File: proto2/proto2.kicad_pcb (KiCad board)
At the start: 2 copper layers, 245.9 x 132.5 mm, 239 parts, among them J1 Output 1, J10 Output, J11 Device, J12 Output, J13 Daughter Card, J2 Main Power, J3 Output, J4 Output, J5 Device, J6 Output, J7 Device, J8 Output, J9 Device, Q1 2N7002, Q10 2N7002, Q11 2N7002, Q12 2N7002, Q13 2N7002, Q14 2N7002, Q2 2N7002, Q3 2N7002, Q4 2N7002, Q5 2N7002, Q6 2N7002, Q7 2N7002, Q8 2N7002, Q9 2N7002, SW1 SW_DIP_x04, U1 AQY282SX, U10 AQY282SX, U11 AQY282SX, U12 AQY282SX, U13 AQY282SX, U14 AQY282SX, U15 NCP59300, U2 AQY282SX, U3 AQY282SX, U4 AQY282SX, U5 AQY282SX, U6 AQY282SX, U7 AQY282SX, U8 AQY282SX, U9 AQY282SX

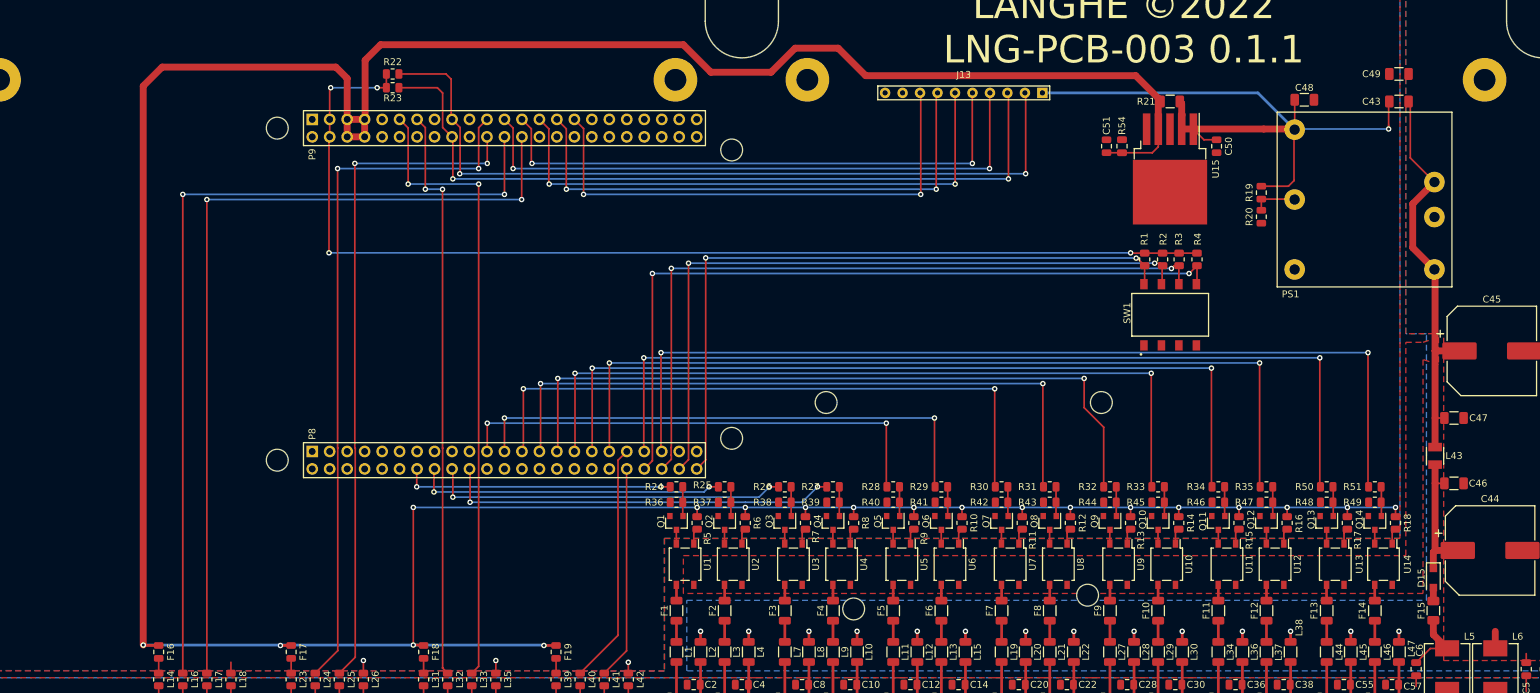
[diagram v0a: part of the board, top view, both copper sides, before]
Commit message: Added switch for 5V external devices power based off SYS_RESETn.
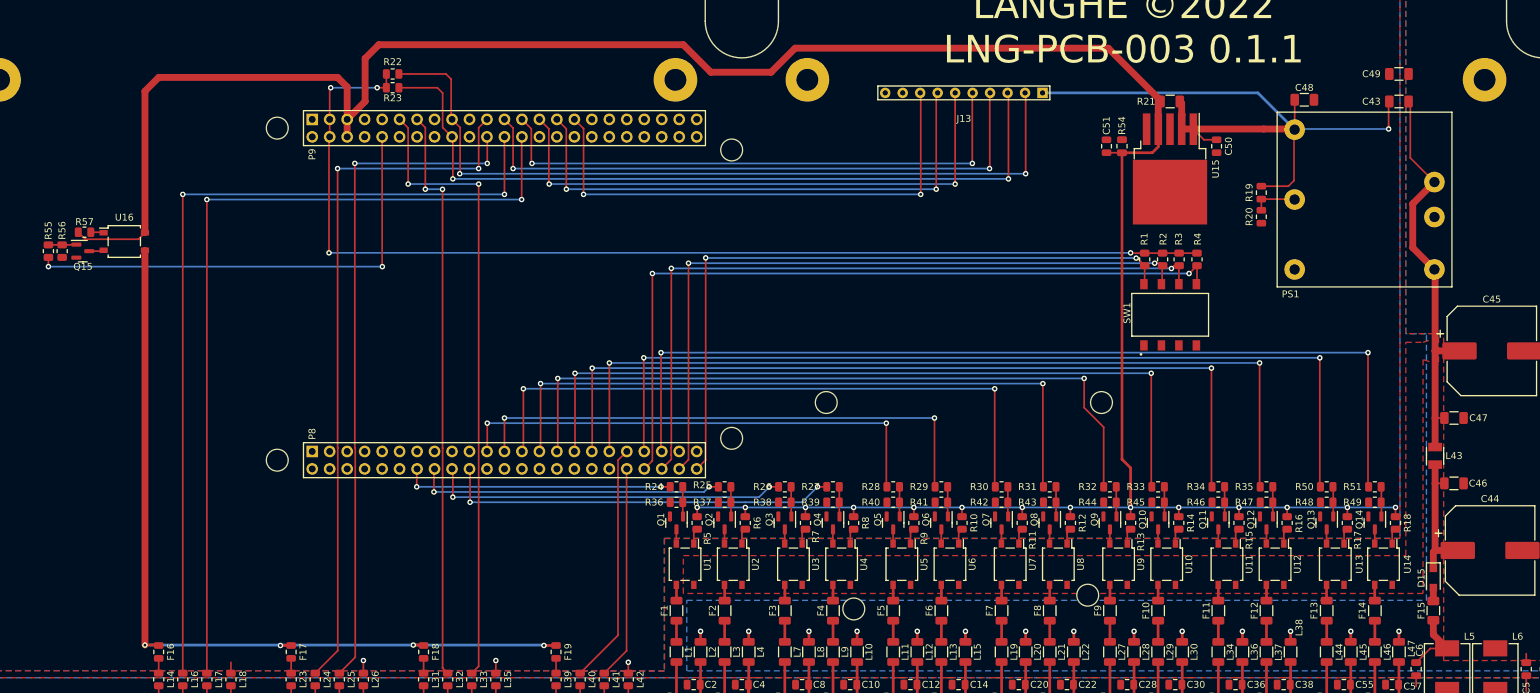
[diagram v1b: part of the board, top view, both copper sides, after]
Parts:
- added Q15: 2N7002, Package_TO_SOT_SMD:SOT-23, F.Cu at (17.0, 81.0)
- added R55: 1K, Resistor_SMD:R_0805_2012Metric, F.Cu at (12.0, 81.0)
- added R56: 27K, Resistor_SMD:R_0805_2012Metric, F.Cu at (14.0, 81.0)
- added R57: 433R, Resistor_SMD:R_0805_2012Metric, F.Cu at (17.2, 78.2)
- added U16: AQY282SX, Package_SO:SO-4_4.4x4.3mm_P2.54mm, F.Cu at (23.0, 79.6)
- D15: value SMA -> D_Small_ALT
- Q13, Q14: footprint Package_BCR:SOT-23 -> Package_TO_SOT_SMD:SOT-23
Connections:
- BB1 pad 9.10: unconnected-(BB1-Pad9.10) -> RESETn
- BB1 pad 9.7: +5V -> unconnected-(BB1-Pad9.7)
- BB1 pad 9.8: +5V -> unconnected-(BB1-Pad9.8)
- F16 pad 2: +5V -> +5VP
- F17 pad 2: +5V -> +5VP
- F18 pad 2: +5V -> +5VP
- F19 pad 2: +5V -> +5VP
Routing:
- net +5V: track 523.2 -> 390.2 mm, vias 19 -> 14
- net +5VP: track 0.00 -> 122.2 mm, vias 0 -> 4
- net RESETn: track 0.00 -> 68.7 mm, vias 0 -> 2
- net Net-(Q15-Pad1): track 0.00 -> 4.08 mm
- net Earth: track 28.2 -> 25.7 mm
- net Net-(Q15-Pad3): track 0.00 -> 2.15 mm
- net Net-(R57-Pad1): track 0.00 -> 1.90 mm

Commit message: Working in suggestions from CFL review.
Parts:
- removed C50: 1uF, Capacitor_SMD:C_0805_2012Metric
- removed R21: 0R, Capacitor_SMD:C_1206_3216Metric
- removed U15: NCP59300, Package_TO_SOT_SMD:TO-263-5_TabPin3
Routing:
- net +5V: track 390.2 -> 195.2 mm
- net VDD: track 98.1 -> 0.75 mm, vias 1 -> 0
- net +5VP: track 122.2 -> 64.8 mm
- net GND: vias 5 -> 6
- added copper zone on In2.Cu, net +5V
- added copper zone on In1.Cu, net GND
- removed copper zone on F.Cu, net GND
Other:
- copper layers 2 -> 4

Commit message: Laying out new filters and some schematic updates.
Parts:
- removed F16, F17, F18, F19: 500mA, Resistor_SMD:R_0805_2012Metric
- removed the J1 at (108.5, 152.5)
- removed the J10 at (187.2, 152.5)
- removed the J12 at (203.0, 152.5)
- removed L37, L38, L44, L45, L46, L47: 1A Ferrite, Resistor_SMD:R_1206_3216Metric
- removed L40, L41: 0R, Resistor_SMD:R_0805_2012Metric
- removed REF**: Langhe_Carrot, BCR_Art:Langhe_Carrot
- removed U16: AQY282SX, Package_SO:SO-4_4.4x4.3mm_P2.54mm
- added C50: 10uF, Capacitor_SMD:C_0805_2012Metric, F.Cu at (134.0, 243.2)
- added C58: 10uF, Capacitor_SMD:C_0805_2012Metric, F.Cu at (86.4, 291.4)
- added C59: 10uF, Capacitor_SMD:C_0805_2012Metric, F.Cu at (99.7, 291.4)
- added C60: 10uF, Capacitor_SMD:C_0805_2012Metric, F.Cu at (154.2, 232.2)
- added C61: 10uF, Capacitor_SMD:C_0805_2012Metric, F.Cu at (103.2, 282.4)
- added C62: 10uF, Capacitor_SMD:C_0805_2012Metric, F.Cu at (137.3, 249.0)
- added C63: 10uF, Capacitor_SMD:C_0805_2012Metric, F.Cu at (154.2, 235.2)
- added C64: 10uF, Capacitor_SMD:C_0805_2012Metric, F.Cu at (90.8, 294.4)
- added C65: 10uF, Capacitor_SMD:C_0805_2012Metric, F.Cu at (86.4, 297.4)
- added C66: 10uF, Capacitor_SMD:C_0805_2012Metric, F.Cu at (141.8, 255.0)
- added C67: 10uF, Capacitor_SMD:C_0805_2012Metric, F.Cu at (140.6, 261.1)
- added C68: 10uF, Capacitor_SMD:C_0805_2012Metric, F.Cu at (158.6, 235.2)
- added C69: 10uF, Capacitor_SMD:C_0805_2012Metric, F.Cu at (122.2, 277.6)
- added C70: 10uF, Capacitor_SMD:C_0805_2012Metric, F.Cu at (95.3, 294.4)
- added C71: 10uF, Capacitor_SMD:C_0805_2012Metric, F.Cu at (95.3, 291.4)
- added C72: 10uF, Capacitor_SMD:C_0805_2012Metric, F.Cu at (157.4, 238.2)
- added C73: 10uF, Capacitor_SMD:C_0805_2012Metric, F.Cu at (136.2, 261.1)
- added C74: 10uF, Capacitor_SMD:C_0805_2012Metric, F.Cu at (140.6, 258.1)
- added C75: 10uF, Capacitor_SMD:C_0805_2012Metric, F.Cu at (146.2, 253.8)
- added C76: 10uF, Capacitor_SMD:C_0805_2012Metric, F.Cu at (113.2, 276.9)
- added C77: 10uF, Capacitor_SMD:C_0805_2012Metric, F.Cu at (151.8, 243.6)
- added C78: 10uF, Capacitor_SMD:C_0805_2012Metric, F.Cu at (128.4, 265.5)
- added C79: 10uF, Capacitor_SMD:C_0805_2012Metric, F.Cu at (157.4, 241.2)
- added C80: 10uF, Capacitor_SMD:C_0805_2012Metric, F.Cu at (90.8, 291.4)
- added C81: 10uF, Capacitor_SMD:C_0805_2012Metric, F.Cu at (86.4, 294.4)
- added C82: 10uF, Capacitor_SMD:C_0805_2012Metric, F.Cu at (163.1, 232.2)
- added C83: 10uF, Capacitor_SMD:C_0805_2012Metric, F.Cu at (128.4, 268.5)
- added C84: 10uF, Capacitor_SMD:C_0805_2012Metric, F.Cu at (132.8, 267.1)
- added C85: 10uF, Capacitor_SMD:C_0805_2012Metric, F.Cu at (123.9, 268.5)
- added C86: 10uF, Capacitor_SMD:C_0805_2012Metric, F.Cu at (193.8, 248.4)
- added C87: 10uF, Capacitor_SMD:C_0805_2012Metric, F.Cu at (219.5, 233.2)
- added C88: 10uF, Capacitor_SMD:C_0805_2012Metric, F.Cu at (215.0, 237.0)
- added C89: 10uF, Capacitor_SMD:C_0805_2012Metric, F.Cu at (210.1, 232.8)
- added C90: 10uF, Capacitor_SMD:C_0805_2012Metric, F.Cu at (198.2, 248.4)
- added C91: 10uF, Capacitor_SMD:C_0805_2012Metric, F.Cu at (193.8, 245.4)
- added C92: 10uF, Capacitor_SMD:C_0805_2012Metric, F.Cu at (214.8, 232.2)
- added C93: 10uF, Capacitor_SMD:C_0805_2012Metric, F.Cu at (198.2, 245.4)
- added C94: 10uF, Capacitor_SMD:C_0805_2012Metric, F.Cu at (189.3, 245.4)
- added C95: 10uF, Capacitor_SMD:C_0805_2012Metric, F.Cu at (189.3, 248.4)
- added J2: Output, Connector_BCR:Phoenix_Contact_PST_4, F.Cu at (108.5, 152.5)
- added J5: Output, Connector_BCR:Phoenix_Contact_PST_4, F.Cu at (155.8, 152.5)
- added J7: Output, Connector_BCR:Phoenix_Contact_PST_4, F.Cu at (124.2, 152.5)
- added PS2: B0505S-1WR3, Converter_DCDC:Converter_DCDC_Murata_MEE1SxxxxSC_THT, F.Cu at (209.6, 245.9)
- added PS3: B0505S-1WR3, Converter_DCDC:Converter_DCDC_Murata_MEE1SxxxxSC_THT, F.Cu at (217.4, 245.9)
- added Q16: AO3401A, Package_TO_SOT_SMD:SOT-23, F.Cu at (-26.2, 97.0)
- added R100: 0R, Resistor_SMD:R_0805_2012Metric, F.Cu at (131.0, 278.9)
- added R101: 0R, Resistor_SMD:R_0805_2012Metric, F.Cu at (150.5, 262.7)
- added R102: 0R, Resistor_SMD:R_0805_2012Metric, F.Cu at (150.7, 256.7)
- added R103: 0R, Resistor_SMD:R_0805_2012Metric, F.Cu at (141.6, 269.9)
- added R104: 0R, Resistor_SMD:R_0805_2012Metric, F.Cu at (153.9, 259.6)
- added R105: 0R, Resistor_SMD:R_0805_2012Metric, F.Cu at (108.5, 291.4)
- added R106: 0R, Resistor_SMD:R_0805_2012Metric, F.Cu at (99.6, 306.2)
- added R107: 0R, Resistor_SMD:R_0805_2012Metric, F.Cu at (95.2, 300.4)
- added R108: 0R, Resistor_SMD:R_0805_2012Metric, F.Cu at (90.8, 303.4)
- added R109: 0R, Resistor_SMD:R_0805_2012Metric, F.Cu at (166.3, 238.2)
- added R110: 0R, Resistor_SMD:R_0805_2012Metric, F.Cu at (146.1, 268.6)
- added R111: 0R, Resistor_SMD:R_0805_2012Metric, F.Cu at (125.5, 243.2)
- added R112: 0R, Resistor_SMD:R_0805_2012Metric, F.Cu at (150.7, 250.8)
- added R113: 0R, Resistor_SMD:R_0805_2012Metric, F.Cu at (159.5, 247.2)
- added R114: 0R, Resistor_SMD:R_0805_2012Metric, F.Cu at (163.9, 247.1)
- added R115: 0R, Resistor_SMD:R_0805_2012Metric, F.Cu at (132.0, 243.2)
- added R116: 0R, Resistor_SMD:R_0805_2012Metric, F.Cu at (137.2, 267.0)
- added R117: 0R, Resistor_SMD:R_0805_2012Metric, F.Cu at (112.9, 294.3)
- added R118: 0R, Resistor_SMD:R_0805_2012Metric, F.Cu at (90.8, 300.4)
- added R119: 0R, Resistor_SMD:R_0805_2012Metric, F.Cu at (108.5, 294.3)
- added R120: 0R, Resistor_SMD:R_0805_2012Metric, F.Cu at (99.6, 300.4)
- added R121: 0R, Resistor_SMD:R_0805_2012Metric, F.Cu at (146.2, 256.8)
- added R122: 0R, Resistor_SMD:R_0805_2012Metric, F.Cu at (180.8, 232.2)
- added R123: 0R, Resistor_SMD:R_0805_2012Metric, F.Cu at (176.3, 235.1)
- added R124: 0R, Resistor_SMD:R_0805_2012Metric, F.Cu at (170.7, 238.1)
- added R125: 0R, Resistor_SMD:R_0805_2012Metric, F.Cu at (126.5, 283.4)
- added R126: 0R, Resistor_SMD:R_0805_2012Metric, F.Cu at (159.5, 250.2)
- added R127: 0R, Resistor_SMD:R_0805_2012Metric, F.Cu at (170.7, 244.1)
- added R128: 0R, Resistor_SMD:R_0805_2012Metric, F.Cu at (155.1, 256.1)
- added R129: 0R, Resistor_SMD:R_0805_2012Metric, F.Cu at (166.3, 241.1)
- added R130: 0R, Resistor_SMD:R_0805_2012Metric, F.Cu at (146.1, 262.7)
- added R131: 0R, Resistor_SMD:R_0805_2012Metric, F.Cu at (137.2, 264.0)
- added R132: 0R, Resistor_SMD:R_0805_2012Metric, F.Cu at (171.9, 232.2)
- added R133: 0R, Resistor_SMD:R_0805_2012Metric, F.Cu at (167.5, 235.2)
- added R134: 0R, Resistor_SMD:R_0805_2012Metric, F.Cu at (155.1, 253.1)
- added R135: 0R, Resistor_SMD:R_0805_2012Metric, F.Cu at (187.5, 287.0)
- added R136: 0R, Resistor_SMD:R_0805_2012Metric, F.Cu at (155.1, 247.2)
- added R137: 4.7K, Resistor_SMD:R_0805_2012Metric, F.Cu at (236.2, 233.2)
- added R138: 4.7K, Resistor_SMD:R_0805_2012Metric, F.Cu at (237.5, 245.0)
- added R139: 120R, Resistor_SMD:R_0805_2012Metric, F.Cu at (244.0, 245.2)
- added R140: 120R, Resistor_SMD:R_0805_2012Metric, F.Cu at (236.2, 239.8)
- added R141: 0R, Resistor_SMD:R_0805_2012Metric, F.Cu at (126.6, 277.5)
- added R142: 0R, Resistor_SMD:R_0805_2012Metric, F.Cu at (116.5, 284.8)
- added R143: 0R, Resistor_SMD:R_0805_2012Metric, F.Cu at (161.9, 241.2)
- added R144: 0R, Resistor_SMD:R_0805_2012Metric, F.Cu at (170.7, 241.1)
- added R145: 0R, Resistor_SMD:R_0805_2012Metric, F.Cu at (141.7, 267.0)
- added R146: 0R, Resistor_SMD:R_0805_2012Metric, F.Cu at (131.0, 281.9)
- added R147: 0R, Resistor_SMD:R_0805_2012Metric, F.Cu at (150.7, 253.8)
- added R148: 0R, Resistor_SMD:R_0805_2012Metric, F.Cu at (159.5, 253.1)
- added R149: 0R, Resistor_SMD:R_0805_2012Metric, F.Cu at (121.1, 295.8)
- added R21: 10K, Resistor_SMD:R_0805_2012Metric, F.Cu at (140.1, 291.4)
- added R58: 0R, Resistor_SMD:R_0805_2012Metric, F.Cu at (129.9, 294.3)
- added R59: 0R, Resistor_SMD:R_0805_2012Metric, F.Cu at (130.4, 291.4)
- added R60: 0R, Resistor_SMD:R_0805_2012Metric, F.Cu at (126.0, 291.4)
- added R61: 1K, Resistor_SMD:R_0805_2012Metric, F.Cu at (237.2, 256.8)
- added R62: 1K, Resistor_SMD:R_0805_2012Metric, F.Cu at (237.2, 253.8)
- added R63: 1K, Resistor_SMD:R_0805_2012Metric, F.Cu at (241.7, 253.8)
- added R64: 1K, Resistor_SMD:R_0805_2012Metric, F.Cu at (246.1, 253.8)
- added R65: 10K, Resistor_SMD:R_0805_2012Metric, F.Cu at (241.7, 256.8)
- added R66: 10K, Resistor_SMD:R_0805_2012Metric, F.Cu at (237.2, 250.8)
- added R67: 10K, Resistor_SMD:R_0805_2012Metric, F.Cu at (246.1, 250.8)
- added R68: 10K, Resistor_SMD:R_0805_2012Metric, F.Cu at (241.7, 250.8)
- added R69: 0R, Resistor_SMD:R_0805_2012Metric, F.Cu at (95.2, 303.4)
- added R70: 0R, Resistor_SMD:R_0805_2012Metric, F.Cu at (99.7, 297.4)
- added R71: 0R, Resistor_SMD:R_0805_2012Metric, F.Cu at (99.6, 303.3)
- added R72: 0R, Resistor_SMD:R_0805_2012Metric, F.Cu at (104.0, 300.4)
- added R73: 0R, Resistor_SMD:R_0805_2012Metric, F.Cu at (103.2, 138.5)
- added R74: 0R, Resistor_SMD:R_0805_2012Metric, F.Cu at (106.8, 138.5)
- added R75: 0R, Resistor_SMD:R_0805_2012Metric, F.Cu at (110.2, 138.5)
- added R76: 0R, Resistor_SMD:R_0805_2012Metric, F.Cu at (113.8, 138.5)
- added R77: 0R, Resistor_SMD:R_0805_2012Metric, F.Cu at (103.2, 144.5)
- added R78: 0R, Resistor_SMD:R_0805_2012Metric, F.Cu at (106.8, 144.5)
- added R79: 0R, Resistor_SMD:R_0805_2012Metric, F.Cu at (110.2, 144.5)
- added R80: 0R, Resistor_SMD:R_0805_2012Metric, F.Cu at (113.8, 144.5)
- added R81: 0R, Resistor_SMD:R_0805_2012Metric, F.Cu at (104.1, 294.4)
- added R82: 0R, Resistor_SMD:R_0805_2012Metric, F.Cu at (95.2, 297.4)
- added R83: 0R, Resistor_SMD:R_0805_2012Metric, F.Cu at (86.3, 303.4)
- added R84: 0R, Resistor_SMD:R_0805_2012Metric, F.Cu at (104.1, 297.3)
- added R85: 0R, Resistor_SMD:R_0805_2012Metric, F.Cu at (166.3, 244.1)
- added R86: 0R, Resistor_SMD:R_0805_2012Metric, F.Cu at (132.8, 270.1)
- added R87: 0R, Resistor_SMD:R_0805_2012Metric, F.Cu at (171.9, 235.2)
- added R88: 0R, Resistor_SMD:R_0805_2012Metric, F.Cu at (127.2, 274.5)
- added R89: 0R, Resistor_SMD:R_0805_2012Metric, F.Cu at (149.5, 259.8)
- added R90: 0R, Resistor_SMD:R_0805_2012Metric, F.Cu at (155.1, 250.2)
- added R91: 0R, Resistor_SMD:R_0805_2012Metric, F.Cu at (140.5, 273.0)
- added R92: 0R, Resistor_SMD:R_0805_2012Metric, F.Cu at (176.3, 232.2)
- added R93: 0R, Resistor_SMD:R_0805_2012Metric, F.Cu at (108.5, 297.3)
- added R94: 0R, Resistor_SMD:R_0805_2012Metric, F.Cu at (104.1, 291.4)
- added R95: 0R, Resistor_SMD:R_0805_2012Metric, F.Cu at (113.0, 291.4)
- added R96: 0R, Resistor_SMD:R_0805_2012Metric, F.Cu at (99.7, 294.4)
- added R97: 0R, Resistor_SMD:R_0805_2012Metric, F.Cu at (122.1, 280.5)
- added R98: 0R, Resistor_SMD:R_0805_2012Metric, F.Cu at (141.7, 264.0)
- added R99: 0R, Resistor_SMD:R_0805_2012Metric, F.Cu at (161.9, 244.1)
- added U15: AMS1117-3.3, Package_TO_SOT_SMD:SOT-223-3_TabPin2, F.Cu at (64.5, 204.0)
- added U17: ISO1540, Package_SO:SOIC-8_3.9x4.9mm_P1.27mm, F.Cu at (71.2, 204.0)
- added U18: NSI8021N, Package_SO:SOIC-8_3.9x4.9mm_P1.27mm, F.Cu at (79.7, 204.0)
- added U19: EL817, Package_SO:SO-4_7.6x3.6mm_P2.54mm, F.Cu at (54.2, 206.8)
- added U20: EL817, Package_SO:SO-4_7.6x3.6mm_P2.54mm, F.Cu at (50.0, 206.8)
- added U21: EL817, Package_SO:SO-4_7.6x3.6mm_P2.54mm, F.Cu at (45.8, 206.8)
- added U22: EL817, Package_SO:SO-4_7.6x3.6mm_P2.54mm, F.Cu at (41.5, 206.8)
- C16, C17, C24, C25, C32, C33, C40, C41: value DNP -> 10uF
- C51: value 47uF -> 10uF
- J1: renamed from J2; footprint BCR_Connector:Phoenix_Contact_PST_4 -> Connector_BCR:Phoenix_Contact_PST_4
- J10: renamed from J7; footprint BCR_Connector:Phoenix_Contact_PST_5 -> Connector_BCR:Phoenix_Contact_PST_5
- J11: renamed from J9; footprint BCR_Connector:Phoenix_Contact_PST_5 -> Connector_BCR:Phoenix_Contact_PST_5
- J12: renamed from J11; footprint BCR_Connector:Phoenix_Contact_PST_5 -> Connector_BCR:Phoenix_Contact_PST_5
- J3, J4, J6, J8: footprint BCR_Connector:Phoenix_Contact_PST_4 -> Connector_BCR:Phoenix_Contact_PST_4
- J9: renamed from J5; footprint BCR_Connector:Phoenix_Contact_PST_5 -> Connector_BCR:Phoenix_Contact_PST_5
- L1, L10, L11, L12, L13, L15, L19, L2, L20, L21, L22, L27, L28, L29, L3, L30, L34, L36, L4, L7, L8, L9: value 1A Ferrite -> 10uH 500mA; footprint Resistor_SMD:R_1206_3216Metric -> Inductor_SMD:L_0805_2012Metric
- L14, L18, L23, L26, L31, L35, L39, L42: value 500mA Ferrite -> 10uH 500mA; footprint Resistor_SMD:R_0805_2012Metric -> Inductor_SMD:L_0805_2012Metric
- L16, L17, L24, L25, L32, L33: value 0R -> 10uH 500mA; footprint Resistor_SMD:R_0805_2012Metric -> Inductor_SMD:L_0805_2012Metric
- L5, L6: value 100R 5A Ferrite -> 2.2uH 7A
- PS1: value CUI_PDQE20_ISOLATED_DCDC -> CUI PDQE20-Q24-S5-D
- R19: value R Trim Up -> R Trim
- R20: value R Trim Down -> R Trim
- R22, R23: value 10K -> 4.7K
- R54: value 500R -> 0R; footprint Capacitor_SMD:C_0805_2012Metric -> Resistor_SMD:R_0805_2012Metric
- R57: value 433R -> 10K
- SW1: footprint BCR_Switch:CUI_DS04-254-2-04BK-SMT -> Button_Switch_BCR:CUI_DS04-254-2-04BK-SMT
- moved R57 246.3 mm to (129.9, 297.3), turned to 0 degrees
- moved R54 234.0 mm to (125.5, 295.8), turned to 0 degrees
- moved C51 175.7 mm to (148.6, 240.6), turned to 0 degrees
- moved C55 165.6 mm to (112.1, 284.2), turned to 0 degrees
- moved C30 158.9 mm to (103.2, 285.4), turned to 0 degrees
- moved C33 154.1 mm to (86.4, 300.4), turned to 0 degrees
- moved C32 151.2 mm to (90.8, 297.4), turned to 0 degrees
- moved C17 148.9 mm to (131.7, 257.4), turned to 0 degrees
- moved C56 147.0 mm to (127.2, 271.5), turned to 0 degrees
- moved C16 146.5 mm to (137.3, 252.0), turned to 0 degrees
- moved C14 144.9 mm to (107.6, 284.2), turned to 0 degrees
- moved C27 143.7 mm to (113.2, 280.0), turned to 0 degrees
- moved C25 142.8 mm to (132.8, 264.1), turned to 0 degrees
- moved C19 141.2 mm to (108.8, 281.2), turned to 0 degrees
- moved C24 140.9 mm to (161.9, 238.2), turned to 0 degrees
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- renumbered REF** to Outline
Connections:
- BB1 pad 8.1: GND -> GND-SIG
- BB1 pad 8.2: GND -> GND-SIG
- BB1 pad 8.37: TX_4 -> unconnected-(BB1-Pad8.37)
- BB1 pad 8.38: RX_4 -> unconnected-(BB1-Pad8.38)
- BB1 pad 9.1: GND -> GND-SIG
- BB1 pad 9.11: RX_3 -> unconnected-(BB1-Pad9.11)
- BB1 pad 9.13: TX_3 -> unconnected-(BB1-Pad9.13)
- BB1 pad 9.17: SCL -> unconnected-(BB1-Pad9.17)
- BB1 pad 9.18: SDA -> unconnected-(BB1-Pad9.18)
- BB1 pad 9.19: unconnected-(BB1-Pad9.19) -> iSCL
- BB1 pad 9.2: GND -> GND-SIG
- BB1 pad 9.20: unconnected-(BB1-Pad9.20) -> iSDA
- BB1 pad 9.21: TX_2 -> unconnected-(BB1-Pad9.21)
- BB1 pad 9.22: RX_2 -> unconnected-(BB1-Pad9.22)
- BB1 pad 9.24: TX_1 -> iTX
- BB1 pad 9.26: RX_1 -> iRX
- BB1 pad 9.43: GND -> GND-SIG
- BB1 pad 9.44: GND -> GND-SIG
- BB1 pad 9.45: GND -> GND-SIG
- BB1 pad 9.46: GND -> GND-SIG
- C1 pad 2: GNDPWR -> GND-PE
- C10 pad 2: GNDPWR -> GND-PE
- C11 pad 2: GNDPWR -> GND-PE
- C12 pad 2: GNDPWR -> GND-PE
- C13 pad 2: GNDPWR -> GND-PE
- C14 pad 2: GNDPWR -> GND-PE
- C15 pad 2: GNDPWR -> GND-PE
- C16 pad 2: GNDPWR -> GND-PE
- C17 pad 2: GNDPWR -> GND-PE
- C18 pad 2: GNDPWR -> GND-PE
- C19 pad 2: GNDPWR -> GND-PE
- C2 pad 2: GNDPWR -> GND-PE
- C20 pad 2: GNDPWR -> GND-PE
- C21 pad 2: GNDPWR -> GND-PE
- C22 pad 2: GNDPWR -> GND-PE
- C23 pad 2: GNDPWR -> GND-PE
- C24 pad 2: GNDPWR -> GND-PE
- C25 pad 2: GNDPWR -> GND-PE
- C26 pad 2: GNDPWR -> GND-PE
- C27 pad 2: GNDPWR -> GND-PE
- C28 pad 2: GNDPWR -> GND-PE
- C29 pad 2: GNDPWR -> GND-PE
- C3 pad 2: GNDPWR -> GND-PE
- C30 pad 2: GNDPWR -> GND-PE
- C31 pad 2: GNDPWR -> GND-PE
- C32 pad 2: GNDPWR -> GND-PE
- C33 pad 2: GNDPWR -> GND-PE
- C34 pad 2: GNDPWR -> GND-PE
- C35 pad 2: GNDPWR -> GND-PE
- C36 pad 2: GNDPWR -> GND-PE
- C37 pad 2: GNDPWR -> GND-PE
- C38 pad 2: GNDPWR -> GND-PE
- C39 pad 2: GNDPWR -> GND-PE
- C4 pad 2: GNDPWR -> GND-PE
- C40 pad 2: GNDPWR -> GND-PE
- C41 pad 2: GNDPWR -> GND-PE
- C42 pad 2: GNDPWR -> GND-PE
- C44 pad 2: Earth -> GND-PWR
- C45 pad 2: Earth -> GND-PWR
- C46 pad 2: Earth -> GND-PWR
- C47 pad 2: Earth -> GND-PWR
- C48 pad 2: GND -> GND-SIG
- C49 pad 1: GND -> GND-SIG
- C49 pad 2: Earth -> GND-PWR
- C5 pad 1: Earth -> Net-(C5-Pad1)
- C5 pad 2: GNDPWR -> GND-PE
- C51 pad 1: +5V -> Net-(C51-Pad1)
- C51 pad 2: GND -> GND-PE
- C52 pad 1: GNDPWR -> GND-PE
- C52 pad 2: GND -> GND-SIG
- C53 pad 1: Earth -> GND-PWR
- C53 pad 2: GNDPWR -> GND-PE
- C54 pad 2: GNDPWR -> GND-PE
- C55 pad 2: GNDPWR -> GND-PE
- C56 pad 2: GNDPWR -> GND-PE
- C57 pad 2: GNDPWR -> GND-PE
- C6 pad 1: VIN -> Net-(C6-Pad1)
- C6 pad 2: GNDPWR -> GND-PE
- C7 pad 2: GNDPWR -> GND-PE
- C8 pad 2: GNDPWR -> GND-PE
- C9 pad 2: GNDPWR -> GND-PE
- D1 pad 1: Net-(C1-Pad1) -> Net-(D1-Pad1)
- D1 pad 2: Net-(C2-Pad1) -> Net-(D1-Pad2)
- D10 pad 1: Net-(C29-Pad1) -> Net-(D10-Pad1)
- D10 pad 2: Net-(C30-Pad1) -> Net-(D10-Pad2)
- D11 pad 1: Net-(C35-Pad1) -> Net-(D11-Pad1)
- D11 pad 2: Net-(C36-Pad1) -> Net-(D11-Pad2)
- D12 pad 1: Net-(C37-Pad1) -> Net-(D12-Pad1)
- D12 pad 2: Net-(C38-Pad1) -> Net-(D12-Pad2)
- D13 pad 1: Net-(C54-Pad1) -> Net-(D13-Pad1)
- D13 pad 2: Net-(C55-Pad1) -> Net-(D13-Pad2)
- D14 pad 1: Net-(C56-Pad1) -> Net-(D14-Pad1)
- D14 pad 2: Net-(C57-Pad1) -> Net-(D14-Pad2)
- D2 pad 1: Net-(C3-Pad1) -> Net-(D2-Pad1)
- D2 pad 2: Net-(C4-Pad1) -> Net-(D2-Pad2)
- D3 pad 1: Net-(C7-Pad1) -> Net-(D3-Pad1)
- D3 pad 2: Net-(C8-Pad1) -> Net-(D3-Pad2)
- D4 pad 1: Net-(C9-Pad1) -> Net-(D4-Pad1)
- D4 pad 2: Net-(C10-Pad1) -> Net-(D4-Pad2)
- D5 pad 1: Net-(C11-Pad1) -> Net-(D5-Pad1)
- D5 pad 2: Net-(C12-Pad1) -> Net-(D5-Pad2)
- D6 pad 1: Net-(C13-Pad1) -> Net-(D6-Pad1)
- D6 pad 2: Net-(C14-Pad1) -> Net-(D6-Pad2)
- D7 pad 1: Net-(C19-Pad1) -> Net-(D7-Pad1)
- D7 pad 2: Net-(C20-Pad1) -> Net-(D7-Pad2)
- D8 pad 1: Net-(C21-Pad1) -> Net-(D8-Pad1)
- D8 pad 2: Net-(C22-Pad1) -> Net-(D8-Pad2)
- D9 pad 1: Net-(C27-Pad1) -> Net-(D9-Pad1)
- D9 pad 2: Net-(C28-Pad1) -> Net-(D9-Pad2)
- J10 pad 1: Net-(C26-Pad1) -> Net-(J10-Pad1)
- J10 pad 2: Net-(C25-Pad1) -> unconnected-(J10-Pad2)
- J10 pad 3: Net-(C24-Pad1) -> unconnected-(J10-Pad3)
- J10 pad 4: Net-(C23-Pad1) -> Net-(J10-Pad4)
- J10 pad 5: GNDPWR -> GND-PE
- J11 pad 1: Net-(C34-Pad1) -> Net-(J11-Pad1)
- J11 pad 2: Net-(C33-Pad1) -> SCL
- J11 pad 3: Net-(C32-Pad1) -> SDA
- J11 pad 4: Net-(C31-Pad1) -> Net-(J11-Pad4)
- J11 pad 5: GNDPWR -> GND-PE
- J12 pad 1: Net-(C42-Pad1) -> Net-(J12-Pad1)
- J12 pad 2: Net-(C41-Pad1) -> TX
- J12 pad 3: Net-(C40-Pad1) -> RX
- J12 pad 4: Net-(C39-Pad1) -> Net-(J12-Pad4)
- J12 pad 5: GNDPWR -> GND-PE
- J13 pad 10: GND -> GND-SIG
- J13 pad 2: SCL -> iSCL
- J13 pad 3: SDA -> iSDA
- J13 pad 9: GND -> GND-SIG
- J3 pad 1: Net-(C7-Pad1) -> Net-(D3-Pad1)
- J3 pad 2: Net-(C8-Pad1) -> Net-(D3-Pad2)
- J3 pad 3: Net-(C9-Pad1) -> Net-(D4-Pad1)
- J3 pad 4: Net-(C10-Pad1) -> Net-(D4-Pad2)
- J4 pad 1: Net-(C11-Pad1) -> Net-(D5-Pad1)
- J4 pad 2: Net-(C12-Pad1) -> Net-(D5-Pad2)
- J4 pad 3: Net-(C13-Pad1) -> Net-(D6-Pad1)
- J4 pad 4: Net-(C14-Pad1) -> Net-(D6-Pad2)
- J6 pad 1: Net-(C19-Pad1) -> Net-(D9-Pad1)
- J6 pad 2: Net-(C20-Pad1) -> Net-(D9-Pad2)
- J6 pad 3: Net-(C21-Pad1) -> Net-(D10-Pad1)
- J6 pad 4: Net-(C22-Pad1) -> Net-(D10-Pad2)
- J8 pad 1: Net-(C27-Pad1) -> Net-(D13-Pad1)
- J8 pad 2: Net-(C28-Pad1) -> Net-(D13-Pad2)
- J8 pad 3: Net-(C29-Pad1) -> Net-(D14-Pad1)
- J8 pad 4: Net-(C30-Pad1) -> Net-(D14-Pad2)
- J9 pad 1: Net-(C18-Pad1) -> Net-(J9-Pad1)
- J9 pad 2: Net-(C17-Pad1) -> unconnected-(J9-Pad2)
- J9 pad 3: Net-(C16-Pad1) -> unconnected-(J9-Pad3)
- J9 pad 4: Net-(C15-Pad1) -> Net-(J9-Pad4)
- J9 pad 5: GNDPWR -> GND-PE
- L1 pad 2: Net-(C1-Pad1) -> Net-(D1-Pad1)
- L10 pad 1: Earth -> GND-PWR
- L10 pad 2: Net-(C10-Pad1) -> Net-(D4-Pad2)
- L11 pad 2: Net-(C11-Pad1) -> Net-(D5-Pad1)
- L12 pad 1: Earth -> GND-PWR
- L12 pad 2: Net-(C12-Pad1) -> Net-(D5-Pad2)
- L13 pad 2: Net-(C13-Pad1) -> Net-(D6-Pad1)
- L14 pad 1: 5V_1 -> Net-(L14-Pad1)
- L14 pad 2: Net-(C18-Pad1) -> Net-(J9-Pad1)
- L15 pad 1: Earth -> GND-PWR
- L15 pad 2: Net-(C14-Pad1) -> Net-(D6-Pad2)
- L16 pad 1: TX_1 -> DQ4_1
- L16 pad 2: Net-(C17-Pad1) -> Net-(D7-Pad1)
- L17 pad 1: RX_1 -> GND-PWR
- L17 pad 2: Net-(C16-Pad1) -> Net-(D7-Pad2)
- L18 pad 1: GND -> Net-(L18-Pad1)
- L18 pad 2: Net-(C15-Pad1) -> Net-(J9-Pad4)
- L19 pad 1: DQ4_1 -> DQ4_2
- L19 pad 2: Net-(C19-Pad1) -> Net-(D8-Pad1)
- L2 pad 1: Earth -> GND-PWR
- L2 pad 2: Net-(C2-Pad1) -> Net-(D1-Pad2)
- L20 pad 1: Earth -> GND-PWR
- L20 pad 2: Net-(C20-Pad1) -> Net-(D8-Pad2)
- L21 pad 1: DQ4_2 -> DQ5_1
- L21 pad 2: Net-(C21-Pad1) -> Net-(D9-Pad1)
- L22 pad 1: Earth -> GND-PWR
- L22 pad 2: Net-(C22-Pad1) -> Net-(D9-Pad2)
- L23 pad 1: 5V_2 -> Net-(L23-Pad1)
- L23 pad 2: Net-(C26-Pad1) -> Net-(J10-Pad1)
- L24 pad 1: TX_2 -> DQ5_2
- L24 pad 2: Net-(C25-Pad1) -> Net-(D10-Pad1)
- L25 pad 1: RX_2 -> GND-PWR
- L25 pad 2: Net-(C24-Pad1) -> Net-(D10-Pad2)
- L26 pad 1: GND -> Net-(L26-Pad1)
- L26 pad 2: Net-(C23-Pad1) -> Net-(J10-Pad4)
- L27 pad 1: DQ5_1 -> DQ6_1
- L27 pad 2: Net-(C27-Pad1) -> Net-(D11-Pad1)
- L28 pad 1: Earth -> GND-PWR
- L28 pad 2: Net-(C28-Pad1) -> Net-(D11-Pad2)
- L29 pad 1: DQ5_2 -> DQ6_2
- L29 pad 2: Net-(C29-Pad1) -> Net-(D12-Pad1)
- L3 pad 2: Net-(C3-Pad1) -> Net-(D2-Pad1)
- L30 pad 1: Earth -> GND-PWR
- L30 pad 2: Net-(C30-Pad1) -> Net-(D12-Pad2)
- L31 pad 1: 5V_3 -> 5V_I2C
- L31 pad 2: Net-(C34-Pad1) -> Net-(J11-Pad1)
- L32 pad 1: TX_3 -> DQ7_1
- L32 pad 2: Net-(C33-Pad1) -> Net-(D13-Pad1)
- L33 pad 1: RX_3 -> GND-PWR
- L33 pad 2: Net-(C32-Pad1) -> Net-(D13-Pad2)
- L34 pad 1: DQ6_1 -> DQ7_2
- L34 pad 2: Net-(C35-Pad1) -> Net-(D14-Pad1)
- L35 pad 1: GND -> GND_I2C
- L35 pad 2: Net-(C31-Pad1) -> Net-(J11-Pad4)
- L36 pad 1: Earth -> GND-PWR
- L36 pad 2: Net-(C36-Pad1) -> Net-(D14-Pad2)
- L39 pad 1: 5V_4 -> 5V_UART
- L39 pad 2: Net-(C42-Pad1) -> Net-(J12-Pad1)
- L4 pad 1: Earth -> GND-PWR
- L4 pad 2: Net-(C4-Pad1) -> Net-(D2-Pad2)
- L42 pad 1: GND -> GND_UART
- L42 pad 2: Net-(C39-Pad1) -> Net-(J12-Pad4)
- L6 pad 1: Earth -> GND-PWR
- L7 pad 2: Net-(C7-Pad1) -> Net-(D3-Pad1)
- L8 pad 1: Earth -> GND-PWR
- L8 pad 2: Net-(C8-Pad1) -> Net-(D3-Pad2)
- L9 pad 2: Net-(C9-Pad1) -> Net-(D4-Pad1)
- PS1 pad 2: Earth -> GND-PWR
- PS1 pad 6: GND -> GND-SIG
- Q1 pad 2: GND -> GND-SIG
- Q10 pad 2: GND -> GND-SIG
- Q11 pad 2: GND -> GND-SIG
- Q12 pad 2: GND -> GND-SIG
- Q13 pad 2: GND -> GND-SIG
- Q14 pad 2: GND -> GND-SIG
- Q15 pad 2: GND -> GND-SIG
- Q2 pad 2: GND -> GND-SIG
- Q3 pad 2: GND -> GND-SIG
- Q4 pad 2: GND -> GND-SIG
- Q5 pad 2: GND -> GND-SIG
- Q6 pad 2: GND -> GND-SIG
- Q7 pad 2: GND -> GND-SIG
- Q8 pad 2: GND -> GND-SIG
- Q9 pad 2: GND -> GND-SIG
- R20 pad 2: GND -> GND-SIG
- R22 pad 2: SCL -> iSCL
- R23 pad 2: SDA -> iSDA
- R36 pad 2: GND -> GND-SIG
- R37 pad 2: GND -> GND-SIG
- R38 pad 2: GND -> GND-SIG
- R39 pad 2: GND -> GND-SIG
- R40 pad 2: GND -> GND-SIG
- R41 pad 2: GND -> GND-SIG
- R42 pad 2: GND -> GND-SIG
- R43 pad 2: GND -> GND-SIG
- R44 pad 2: GND -> GND-SIG
- R45 pad 2: GND -> GND-SIG
- R46 pad 2: GND -> GND-SIG
- R47 pad 2: GND -> GND-SIG
- R48 pad 2: GND -> GND-SIG
- R49 pad 2: GND -> GND-SIG
- R52 pad 1: GNDPWR -> GND-PE
- R52 pad 2: GND -> GND-SIG
- R53 pad 1: Earth -> GND-PWR
- R53 pad 2: GNDPWR -> GND-PE
- R54 pad 1: GND -> /Power/24V_POUR
- R54 pad 2: +5V -> GND-PWR
- R56 pad 2: GND -> GND-SIG
- R57 pad 1: Net-(R57-Pad1) -> +5V
- R57 pad 2: +5V -> Net-(Q15-Pad3)
- SW1 pad 1: GND -> GND-SIG
- SW1 pad 2: GND -> GND-SIG
- SW1 pad 3: GND -> GND-SIG
- SW1 pad 4: GND -> GND-SIG
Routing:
- net TX_1: track 124.7 -> 0.00 mm, vias 2 -> 0
- net RX_1: track 123.7 -> 0.00 mm, vias 2 -> 0
- net iSCL: track 0.00 -> 116.1 mm, vias 0 -> 2
- net SCL: track 116.1 -> 0.00 mm, vias 2 -> 0
- net iSDA: track 0.00 -> 112.8 mm, vias 0 -> 2
- net SDA: track 112.8 -> 0.00 mm, vias 2 -> 0
- net TX_2: track 102.9 -> 0.00 mm, vias 2 -> 0
- net RX_2: track 98.2 -> 0.00 mm, vias 2 -> 0
- net RX_3: track 91.7 -> 0.00 mm, vias 2 -> 0
- net TX_3: track 83.8 -> 0.00 mm, vias 2 -> 0
- net unconnected-(BB1-Pad9.21): track 0.00 -> 68.8 mm, vias 0 -> 2
- net +5VP: track 64.8 -> 0.00 mm, vias 4 -> 0
- net unconnected-(BB1-Pad9.22): track 0.00 -> 64.5 mm, vias 0 -> 2
- net iTX: track 0.00 -> 55.1 mm, vias 0 -> 2
- net iRX: track 0.00 -> 54.9 mm, vias 0 -> 2
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- added copper zone on F.Cu, net (none)
- added copper zone on B.Cu, net GND-PE
- added copper zone on B.Cu, net GND-PWR
- added copper zone on F.Cu, net GND-PWR
- added copper zone on B.Cu, net GND-SIG
- added copper zone on In1.Cu, net GND-SIG
- removed copper zone on B.Cu, net Earth
- removed copper zone on F.Cu, net Earth
- removed copper zone on B.Cu, net GND
- removed copper zone on In1.Cu, net GND
- removed copper zone on B.Cu, net GNDPWR
- removed copper zone on F.Cu, net GNDPWR
